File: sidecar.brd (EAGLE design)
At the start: 19.5 x 22.5 mm, 13 parts, among them IC10 LM1117-2-SOT223, IC8 74LVC1G125DBV

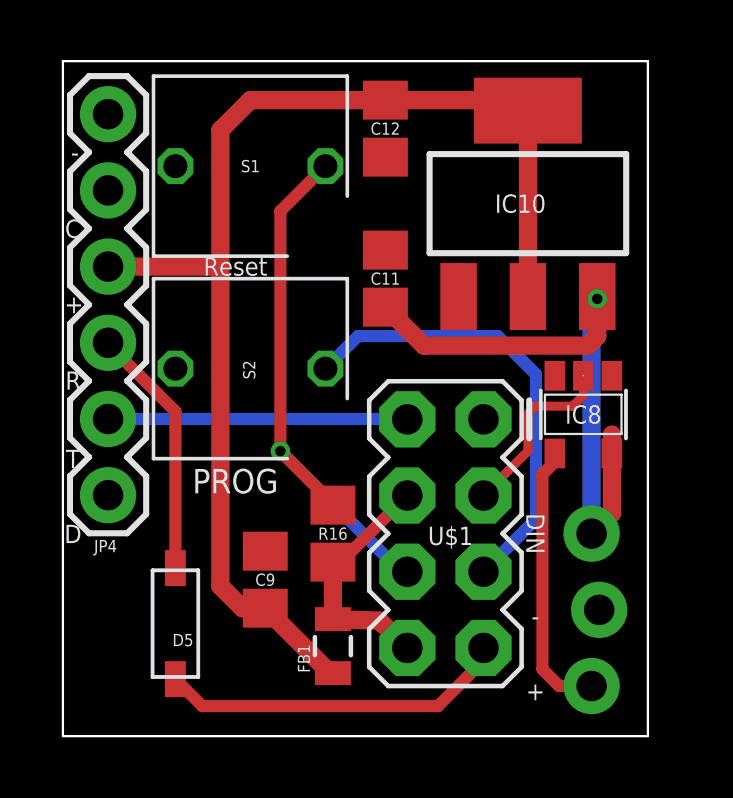
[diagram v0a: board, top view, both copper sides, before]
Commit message: Transistor version
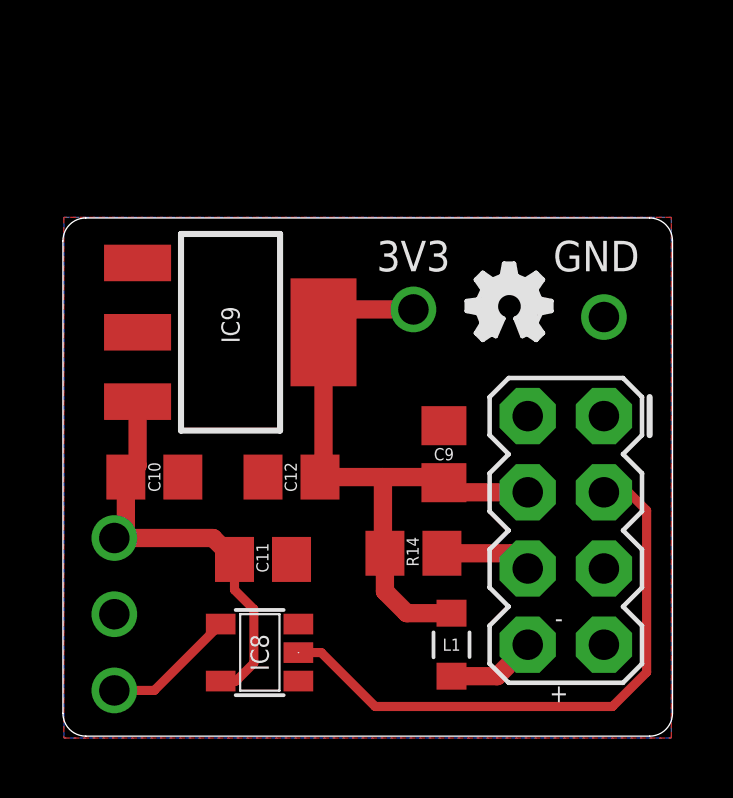
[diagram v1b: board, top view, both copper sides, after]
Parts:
- removed D5: 1N4148, diode:SOD-123
- removed FB1: FB, SparkFun-Passives:0805
- removed IC10: LM1117-2-SOT223, regulators:SOT-223-3
- removed JP3: (no value), connectors:1X03_LOCK
- removed JP4: (no value), headers:1X06
- removed R16: 10k, rcl:R0805
- removed S1, S2: (no value), switch:TACT_5MM
- removed U$1: M04X2ESP, headers:2X4-ESP
- added C10: 10uF, rcl:C0805
- added HDR2: M04X2ESP, headers:2X4-ESP
- added IC9: LM1117-2-SOT223, regulators:SOT-223-3
- added J3: 22-05-7038-03, headers:7395-03
- added L1: (no value), Wurth_Elektronik_Passive_rev19b:WE-CBA_0805(W=3)
- added R14: 10k, rcl:R0805
- added TP23, TP24: TEST_PINTP-2, headers:TP-2
- added U$8: (no value), ohw-logo:OSHW_FILLX100_NOTEXT
- C11, C9: value (none) -> .1uF
- C12: value (none) -> 10uF
- moved IC8 13.4 mm to (6.56, 2.79), turned to 90 degrees
- moved C12 12.0 mm to (7.62, 8.64), turned to 180 degrees
- moved C11 10.2 mm to (6.67, 5.89), turned to 0 degrees
- moved C9 7.28 mm to (12.7, 9.40)
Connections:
- removed net CTS: JP4.2
- removed net DTR: JP4.6
- removed net N$8: D5.C, JP4.4
- net +3V3: now also HDR2.6, IC9.4, L1.1, R14.2, TP24.P$1; no longer FB1.1, IC10.2, IC10.4, JP4.3
- net +5V: now also C10.1, IC9.3, J3.1; no longer IC10.3, JP3.1
- net DIN-IN: now also J3.3; no longer JP3.3
- net GND: now also C10.2, HDR2.1, IC9.1, J3.2, TP23.P$1; no longer IC10.1, JP3.2, JP4.1, S1.2, S2.2, U$1.1
- net GPIO0: now also HDR2.3; no longer S2.1, U$1.3
- net GPIO2: now also HDR2.2; no longer U$1.2
- net RST: now also HDR2.7, R14.1; no longer R16.1, S1.1, U$1.7
- net RXD: now also HDR2.4; no longer D5.A, U$1.4
- net TXD: now also HDR2.5; no longer JP4.5, U$1.5
- net VCC: now also HDR2.8, L1.2; no longer FB1.2, R16.2, U$1.6, U$1.8
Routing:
- net +3V3: track 40.9 -> 21.7 mm
- net RST: track 18.5 -> 3.07 mm, vias 1 -> 0
- net GPIO0: track 15.3 -> 0.00 mm
- net GPIO2: track 6.10 -> 19.9 mm
- net RXD: track 11.7 -> 0.00 mm
- net TXD: track 9.98 -> 0.00 mm
- net N$8: track 8.44 -> 0.00 mm
- net +5V: track 20.7 -> 14.2 mm, vias 1 -> 0
- net VCC: track 8.19 -> 2.99 mm
- net DIN-IN: track 9.23 -> 4.46 mm
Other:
- board size 19.5 x 22.5 mm -> 20.3 x 17.3 mm
- board text added: "3V3"
- board text added: "GND"
- board text removed: "C"
- board text removed: "C1"
- board text removed: "C2"
- board text removed: "C3"
- board text removed: "C4"
- board text removed: "C5"
- board text removed: "C6"
- board text removed: "C7"
- board text removed: "D"
- board text removed: "D1"
- board text removed: "D2"
- board text removed: "D3"
- board text removed: "D4"
- board text removed: "DIN"
- board text removed: "IC1"
- board text removed: "IC2"
- board text removed: "IC3"
- board text removed: "IC4"
- board text removed: "IC5"
- board text removed: "IC6"
- board text removed: "IC7"
- board text removed: "L1"
- board text removed: "L2"
- board text removed: "L3"
- board text removed: "L4"
- board text removed: "Measurements in mm"
- board text removed: "PROG"
- board text removed: "R"
- board text removed: "R1"
- board text removed: "R10"
- board text removed: "R11"
- board text removed: "R12"
- board text removed: "R2"
- board text removed: "R3"
- board text removed: "R4"
- board text removed: "R5"
- board text removed: "R6"
- board text removed: "R7"
- board text removed: "R8"
- board text removed: "R9"
- board text removed: "Reset"
- board text removed: "T"
